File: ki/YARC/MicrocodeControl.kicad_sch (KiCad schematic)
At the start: 24 parts

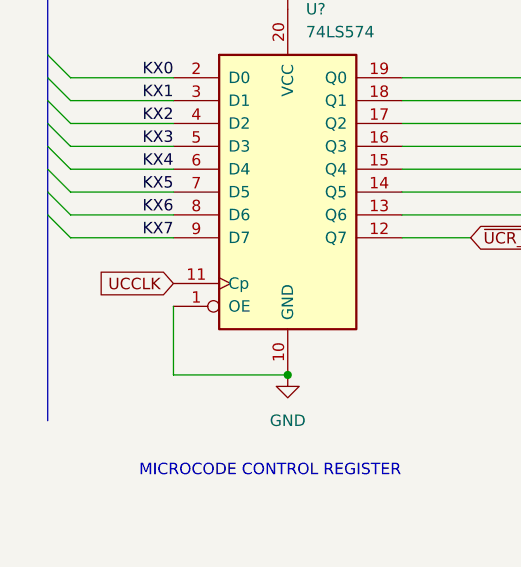
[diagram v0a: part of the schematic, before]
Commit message: All the changes related to the mid-December 2022 K register problem
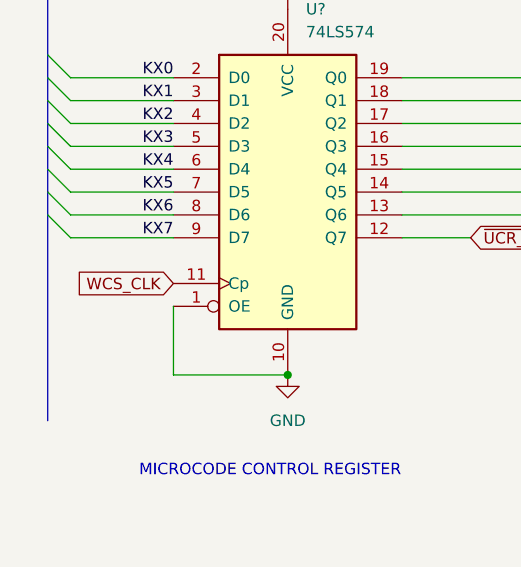
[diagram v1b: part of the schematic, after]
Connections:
- net UCCLK renamed WCS_CLK
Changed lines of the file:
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@@
     )
   )
-  (global_label "UCCLK" (shape input) (at 30.48 53.34 180) (fields_autoplaced)
+  (global_label "WCS_CLK" (shape input) (at 30.48 53.34 180) (fields_autoplaced)
     (effects (font (size 1.27 1.27)) (justify right))
-    (property "Intersheet References" "${INTERSHEET_REFS}" (id 0) (at 21.8983 53.2606 0)
+    (property "Intersheet References" "${INTERSHEET_REFS}" (id 0) (at 19.6002 53.2606 0)
       (effects (font (size 1.27 1.27)) (justify right) hide)
     )
@@
       (effects (font (size 1.27 1.27)) hide)
     )
-    (pin "1")
-    (pin "2")
-    (pin "3")
+    (pin "10")
+    (pin "8")
+    (pin "9")
   )
   (symbol (lib_id "74xx:74LS157") (at 81.28 116.84 0)
@@
       (effects (font (size 1.27 1.27)) hide)
     )
-    (pin "1")
-    (pin "2")
-    (pin "3")
+    (pin "11")
+    (pin "12")
+    (pin "13")
   )
   (symbol (lib_id "power:VCC") (at 154.94 143.51 0)
@@
       (effects (font (size 1.27 1.27)) hide)
     )
-    (pin "1")
-    (pin "2")
-    (pin "3")
+    (pin "11")
+    (pin "12")
+    (pin "13")
   )
   (symbol (lib_id "power:GND") (at 137.16 113.03 0)
@@
       (effects (font (size 1.27 1.27)) hide)
     )
-    (pin "1")
-    (pin "2")
-    (pin "3")
+    (pin "11")
+    (pin "12")
+    (pin "13")
   )
   (symbol (lib_id "74xx:74LS32") (at 180.34 156.21 0)
@@
       (effects (font (size 1.27 1.27)) hide)
     )
-    (pin "1")
-    (pin "2")
-    (pin "3")
+    (pin "14")
+    (pin "7")
   )
   (symbol (lib_id "74xx:74LS32") (at 162.56 156.21 0)
@@
       (effects (font (size 1.27 1.27)) hide)
     )
-    (pin "1")
-    (pin "2")
-    (pin "3")
+    (pin "14")
+    (pin "7")
   )
   (symbol (lib_id "74xx:74LS157") (at 186.69 41.91 0)
@@
       (effects (font (size 1.27 1.27)) hide)
     )
-    (pin "1")
-    (pin "2")
-    (pin "3")
+    (pin "4")
+    (pin "5")
+    (pin "6")
   )
   (symbol (lib_id "power:VCC") (at 68.58 156.21 0)
@@
       (effects (font (size 1.27 1.27)) hide)
     )
-    (pin "1")
-    (pin "2")
-    (pin "3")
+    (pin "4")
+    (pin "5")
+    (pin "6")
   )
   (symbol (lib_id "power:GND") (at 43.18 63.5 0)
@@
       (effects (font (size 1.27 1.27)) hide)
     )
-    (pin "1")
-    (pin "2")
-    (pin "3")
+    (pin "10")
+    (pin "8")
+    (pin "9")
   )
   (symbol (lib_id "power:VCC") (at 186.69 19.05 0)
@@
       (effects (font (size 1.27 1.27)) hide)
     )
-    (pin "1")
-    (pin "2")
-    (pin "3")
+    (pin "10")
+    (pin "8")
+    (pin "9")
   )
   (symbol (lib_id "74xx:74LS32") (at 220.98 24.13 0)
@@
     (pin "16")
     (pin "8")
-    (pin "1")
-    (pin "2")
-    (pin "3")
+    (pin "10")
+    (pin "11")
+    (pin "12")
+    (pin "13")
+    (pin "14")
+    (pin "15")
+    (pin "9")
+  )
+  (symbol (lib_id "power:VCC") (at 52.07 179.07 0)
+    (in_bom yes) (on_board yes)
+    (property "Reference" "#PWR?" (id 0) (at 52.07 182.88 0)
+      (effects (font (size 1.27 1.27)) hide)
+    )
+    (property "Value" "VCC" (id 1) (at 54.61 179.07 0))
+    (property "Footprint" "" (id 2) (at 52.07 179.07 0)
+      (effects (font (size 1.27 1.27)) hide)
+    )
+    (property "Datasheet" "" (id 3) (at 52.07 179.07 0)
+      (effects (font (size 1.27 1.27)) hide)
+    )
+    (pin "1")
+  )
+  (symbol (lib_id "74xx:74LS32") (at 234.95 77.47 0)
+    (in_bom yes) (on_board yes)
+    (property "Reference" "U?" (id 0) (at 240.03 72.39 0))
+    (property "Value" "74LS32" (id 1) (at 234.95 77.47 0))
+    (property "Footprint" "" (id 2) (at 234.95 77.47 0)
+      (effects (font (size 1.27 1.27)) hide)
+    )
+    (property "Datasheet" "http://www.ti.com/lit/gpn/sn74LS32" (id 3) (at 234.95 77.47 0)
+      (effects (font (size 1.27 1.27)) hide)
+    )
     (pin "4")
     (pin "5")
     (pin "6")
-    (pin "7")
-  )
-  (symbol (lib_id "power:VCC") (at 52.07 179.07 0)
-    (in_bom yes) (on_board yes)
-    (property "Reference" "#PWR?" (id 0) (at 52.07 182.88 0)
-      (effects (font (size 1.27 1.27)) hide)
-    )
-    (property "Value" "VCC" (id 1) (at 54.61 179.07 0))
-    (property "Footprint" "" (id 2) (at 52.07 179.07 0)
-      (effects (font (size 1.27 1.27)) hide)
-    )
-    (property "Datasheet" "" (id 3) (at 52.07 179.07 0)
-      (effects (font (size 1.27 1.27)) hide)
-    )
-    (pin "1")
-  )
-  (symbol (lib_id "74xx:74LS32") (at 234.95 77.47 0)
-    (in_bom yes) (on_board yes)
-    (property "Reference" "U?" (id 0) (at 240.03 72.39 0))
-    (property "Value" "74LS32" (id 1) (at 234.95 77.47 0))
-    (property "Footprint" "" (id 2) (at 234.95 77.47 0)
-      (effects (font (size 1.27 1.27)) hide)
-    )
-    (property "Datasheet" "http://www.ti.com/lit/gpn/sn74LS32" (id 3) (at 234.95 77.47 0)
-      (effects (font (size 1.27 1.27)) hide)
-    )
-    (pin "1")
-    (pin "2")
-    (pin "3")
   )
   (symbol (lib_id "74xx:74LS32") (at 219.71 111.76 0)
@@
       (effects (font (size 1.27 1.27)) hide)
     )
-    (pin "1")
-    (pin "2")
-    (pin "3")
+    (pin "14")
+    (pin "7")
   )
 )

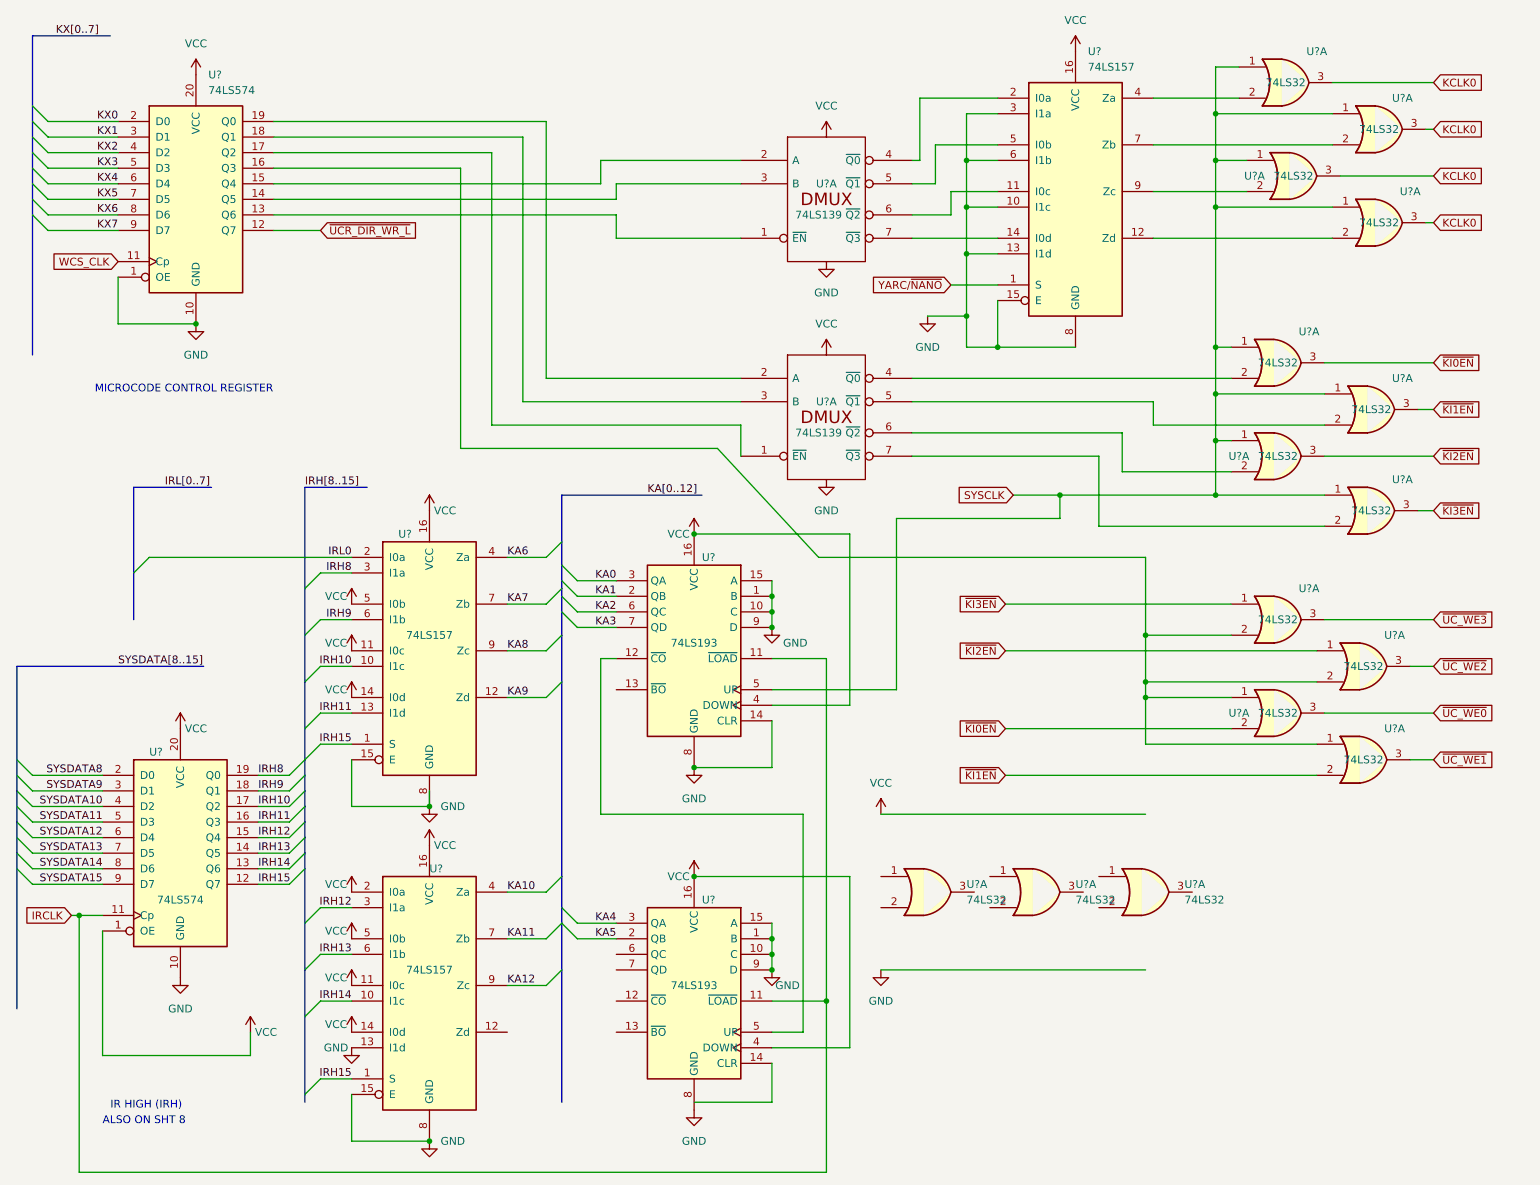
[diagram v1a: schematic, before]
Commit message: Assign part labels (U-numbers) in KiCad and start adding them to Fritzing layouts
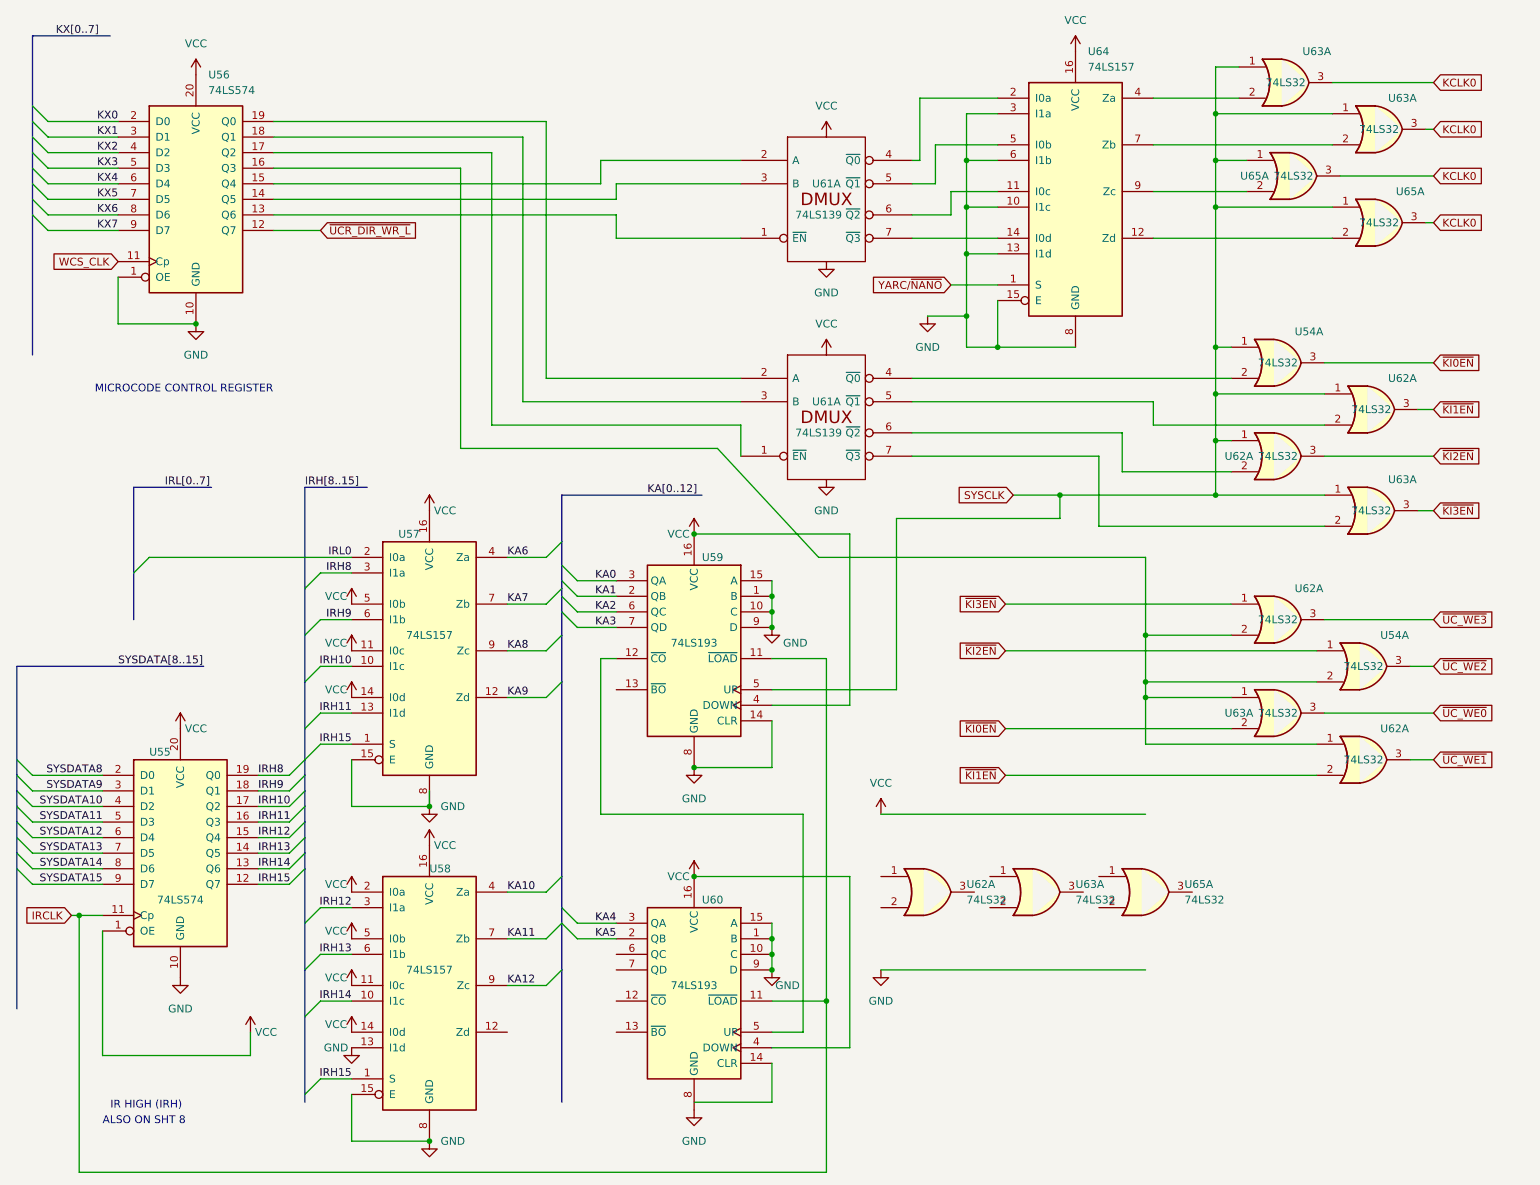
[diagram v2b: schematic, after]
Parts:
- gave numbers to parts that had none: 12

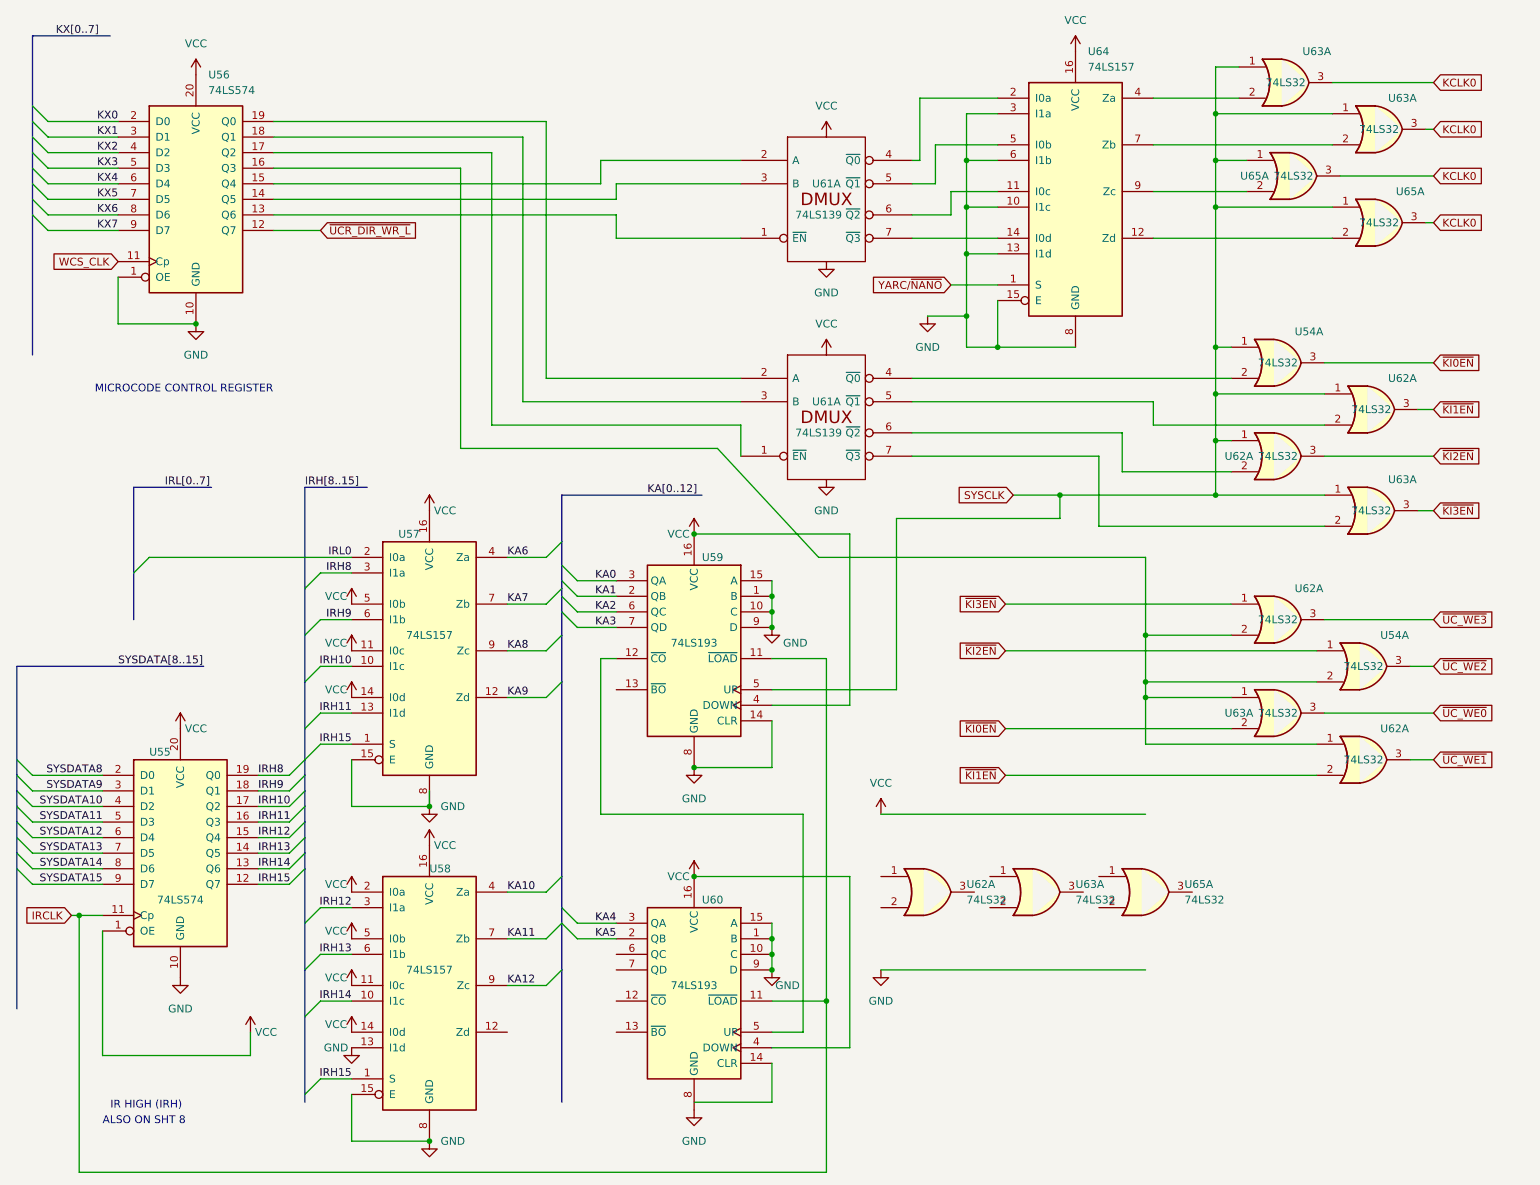
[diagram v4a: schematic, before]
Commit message: ALU schematic checking complete. Ready to start layout.
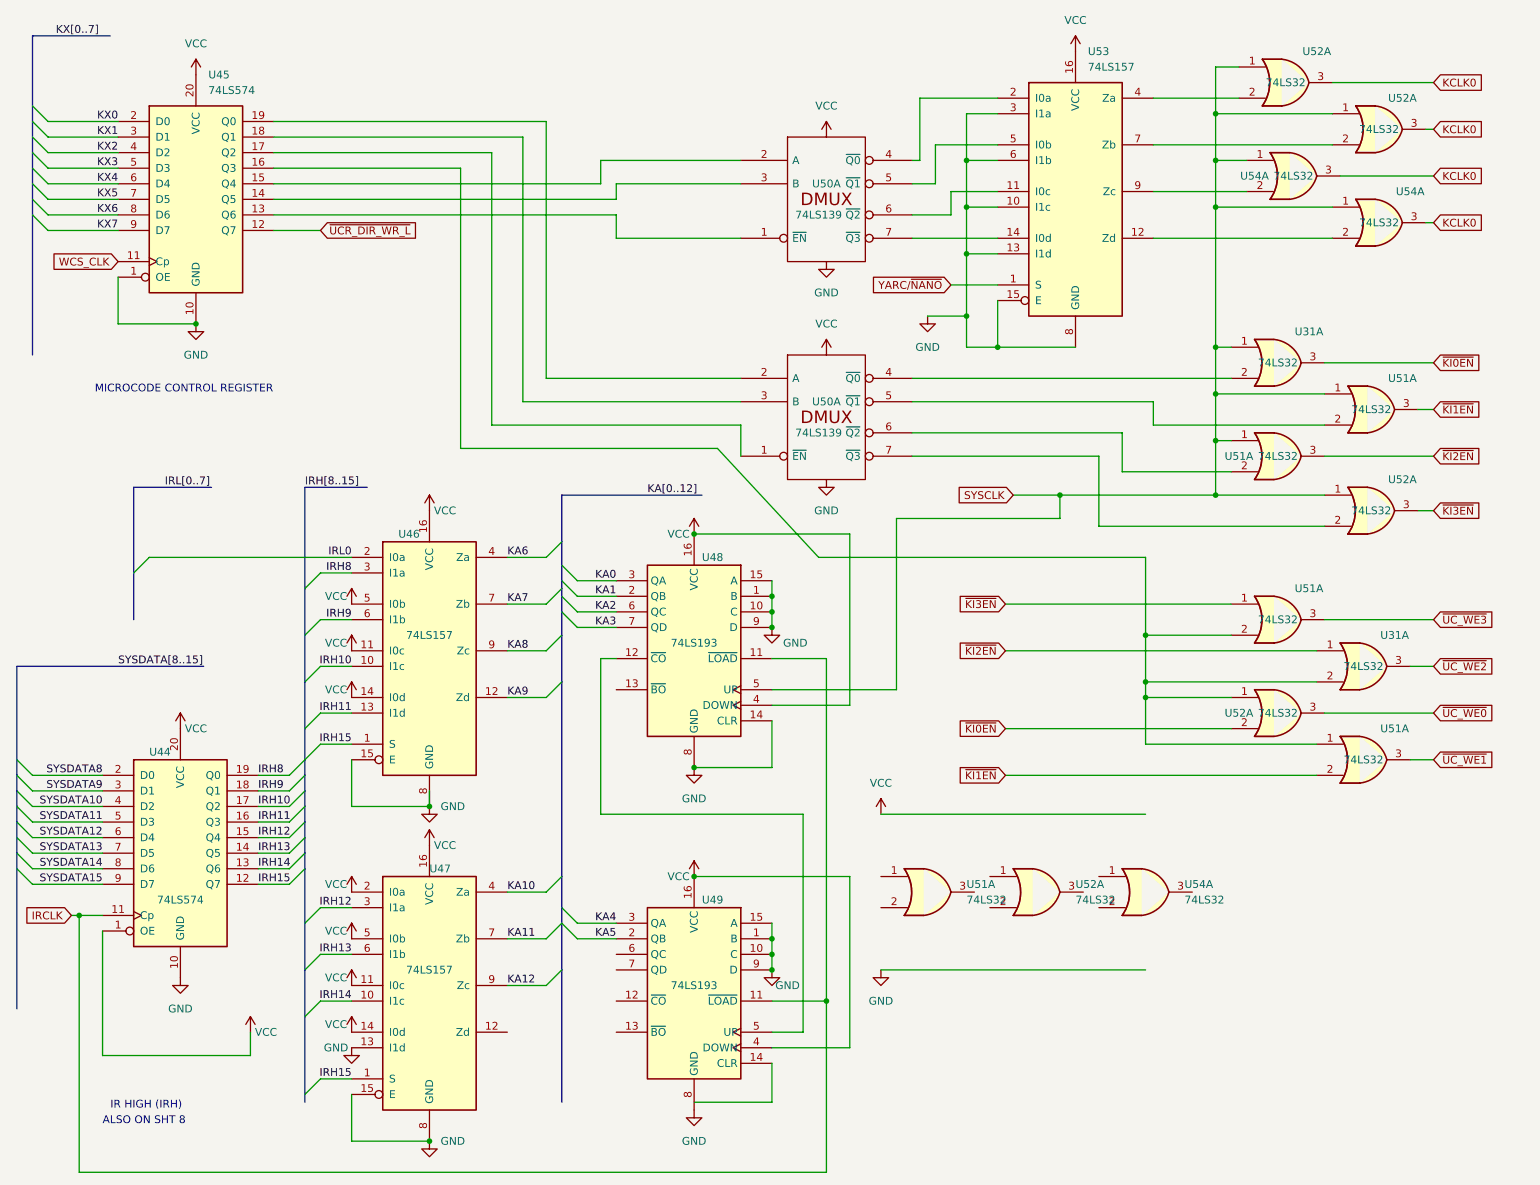
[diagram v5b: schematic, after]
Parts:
- renumbered U54 to U31, U55 to U44, U56 to U45, U57 to U46, U58 to U47, U59 to U48, U60 to U49, U61 to U50, U62 to U51, U63 to U52, U64 to U53, U65 to U54
